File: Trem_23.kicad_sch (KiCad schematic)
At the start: 70 parts, among them J1 +9V, J2 GND, J3 IN, J4 IN GND, J5 OUT, J6 OUT GND, J7 LED SW, J8 LED GND, Q1 MMBT5089, Q2 MBT3904DW1, Q3 MBT3904DW1, Q4 MMBT3906, SW1 SQ/TRI, U1 TL064

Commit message: Trem v2.0: 9 mm pots (correct direction), RANGE switch, LFO-rate LED, 1x4 header; Unit #1 build log
As ordered from JLCPCB 2026-10-04.

Co-Authored-By: Claude Opus 5.5 <noreply@anthropic.com>
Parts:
- removed J3: IN, TestPoint:TestPoint_THTPad_D1.5mm_Drill0.7mm, symbol Connector_Generic:Conn_01x01
- removed J5: OUT, TestPoint:TestPoint_THTPad_D1.5mm_Drill0.7mm, symbol Connector_Generic:Conn_01x01
- removed J7: LED SW, TestPoint:TestPoint_THTPad_D1.5mm_Drill0.7mm, symbol Connector_Generic:Conn_01x01
- removed J8: LED GND, TestPoint:TestPoint_THTPad_D1.5mm_Drill0.7mm, symbol Connector_Generic:Conn_01x01
- added C17: 470n, Capacitor_SMD:C_0805_2012Metric_Pad1.18x1.45mm_HandSolder, symbol Device:C
- added C18: 33n, Capacitor_SMD:C_0805_2012Metric_Pad1.18x1.45mm_HandSolder, symbol Device:C
- added C19: 10n, Capacitor_SMD:C_0805_2012Metric_Pad1.18x1.45mm_HandSolder, symbol Device:C
- added C20: 100n, Capacitor_SMD:C_0805_2012Metric_Pad1.18x1.45mm_HandSolder, symbol Device:C
- added J9: IN/LED/GND/OUT, Connector_PinHeader_2.54mm:PinHeader_1x04_P2.54mm_Vertical, symbol Connector_Generic:Conn_01x04
- added Q5: MMBT3904, Package_TO_SOT_SMD:SOT-23, symbol Transistor_BJT:MMBT3904
- added R33: 2M2, Resistor_SMD:R_0805_2012Metric_Pad1.20x1.40mm_HandSolder, symbol Device:R
- added R34: 47k, Resistor_SMD:R_0805_2012Metric_Pad1.20x1.40mm_HandSolder, symbol Device:R
- added R35: 10k, Resistor_SMD:R_0805_2012Metric_Pad1.20x1.40mm_HandSolder, symbol Device:R
- added SW2: LFO/AUDIO, Trem:SW_Taiway_200_SPDT, symbol Switch:SW_SPDT
- added U2: CD4053, Package_SO:SOIC-16_3.9x9.9mm_P1.27mm, symbol Analog_Switch:CD4053B
- C14: value 10p -> 22p; LCSC C157608 -> C1804
- C3: footprint Capacitor_SMD:CP_Elec_8x10.5 -> Capacitor_THT:CP_Radial_D8.0mm_P3.50mm; now left out of the parts list
- C6: value 470n -> 10n; LCSC C13967 -> C1710
- C7: value 33n -> 1n; LCSC C1739 -> C46653
- C8: value 10n -> 220p; LCSC C1710 -> C107145
- D2, SW1: now left out of the parts list
- J1, J2, J4, J6: footprint TestPoint:TestPoint_THTPad_D1.5mm_Drill0.7mm -> Connector_Wire:SolderWire-0.5sqmm_1x01_D0.9mm_OD2.1mm
- Q2, Q3, RV4: FT Rotation Offset (none) -> 180
- Q4: value MMBT3906 -> MMBT5401; LCSC C84105 -> C8326
- R13: value 270k -> 220k; LCSC C17589 -> C17556
- R17: value 4M7 -> 2M2; LCSC C17674 -> C26113
- RV1, RV2, RV3: footprint Potentiometer_THT:Potentiometer_Omeg_PC16BU_Vertical -> Potentiometer_THT:Potentiometer_Alpha_RD901F-40-00D_Single_Vertical; now left out of the parts list
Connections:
- net +9V: now also C20.1, Q5.3 (C), R34.1, SW2.3 (C), U2.16 (VDD); no longer D2.2 (A), R13.1
- net GND: now also C20.2, J9.3 (Pin_3), SW2.1 (A), U2.6 (INH), U2.7 (VEE), U2.8 (VSS)
- net IN: now also J9.1 (Pin_1)
- net LED_K: now also J9.2 (Pin_2)
- net OUT: now also J9.4 (Pin_4)
- net SQR: now also C18.1
- net TRI: now also C17.1, R35.1
- net DEP_OUT: now reaches C8.2, R12.2, R14.1, U1.1
- net DEP_OUT: now also C19.1
- net SCH_N: now reaches C7.1, R8.2, U1.9 (-)
- net SCH_N: now also U2.1 (B1)
- net INT_N: now reaches C6.1, R5.2, U1.13 (-)
- net INT_N: now also U2.13 (A1)
- net at C10.1, Q1.1 (B), R16.2: now also R33.2; no longer R17.1
- net DEP_N: now reaches C8.1, R11.2, R12.1, R13.2, U1.2 (-)
- net DEP_N: now also U2.3 (C1)
- new net: C18.2, U2.15 (B)
- new net: SW2.2 (B), U2.10 (S2), U2.11 (S1), U2.9 (S3)
- new net: R13.1, R34.2
- new net: R17.1, R33.1
- new net: Q5.1 (B), R35.2
- new net: D2.2 (A), Q5.2 (E)
- new net: C17.2, U2.14 (A)
- new net: C19.2, U2.4 (C)
- no-connect marks 1 -> 4
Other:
- note added: "LFO: SW2 to +9V adds C17-C19 (~2-17 Hz). AUDIO: ~100-800 Hz."
- note added: "RANGE (U2 CD4053)"

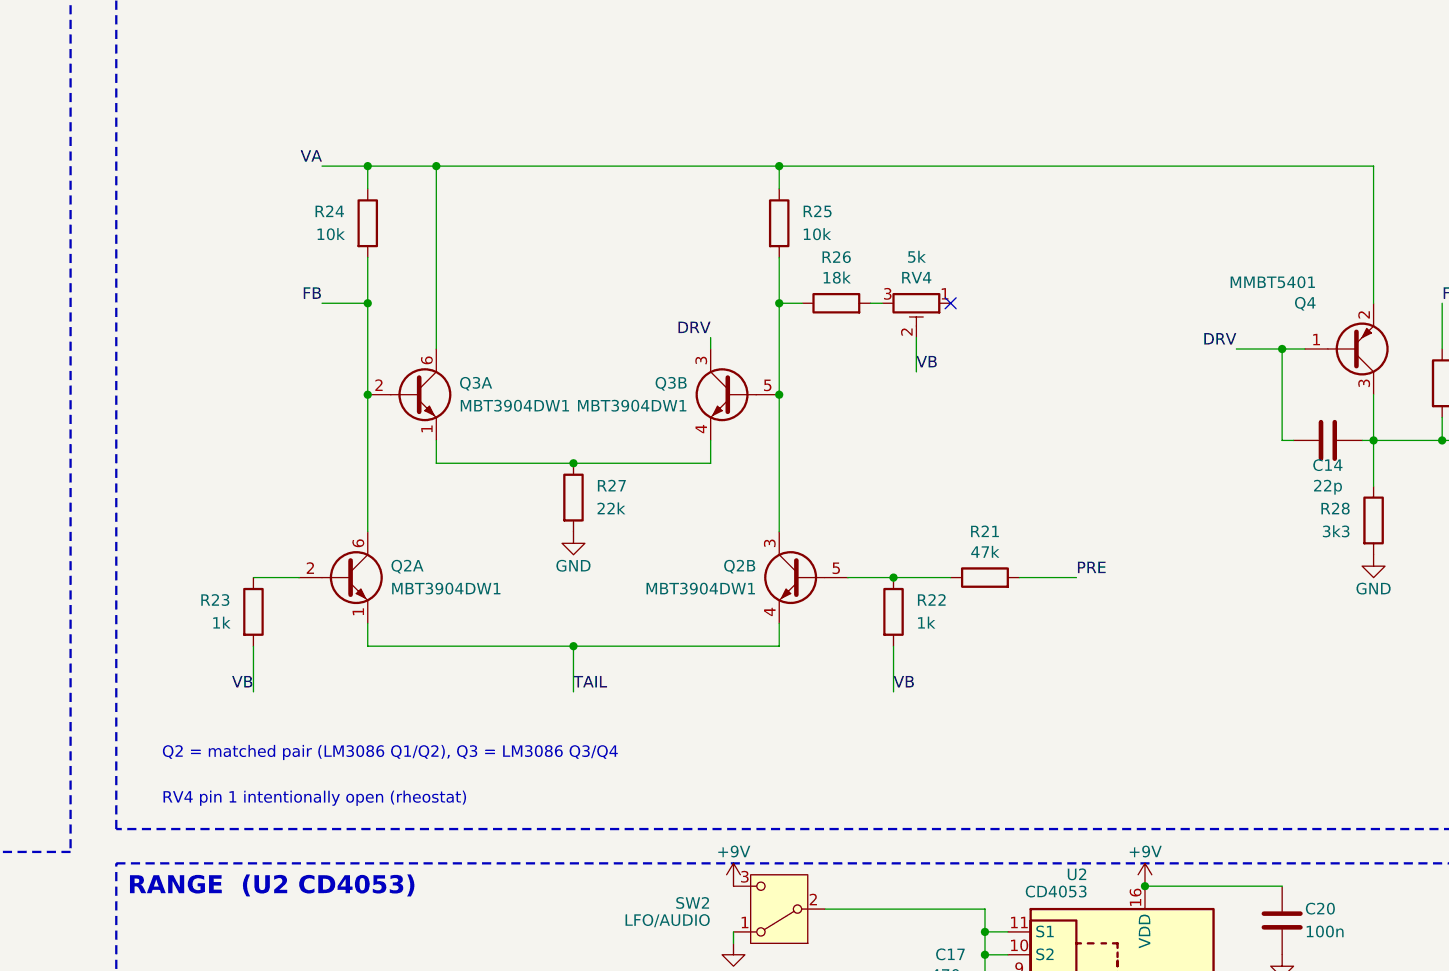
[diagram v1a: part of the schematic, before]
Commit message: v2.1 schematic: symmetric VCA balance trim (RV4 3296W 2k, wiper to VA; R26 20k to VB)
Co-Authored-By: Claude Opus 5.5 <noreply@anthropic.com>
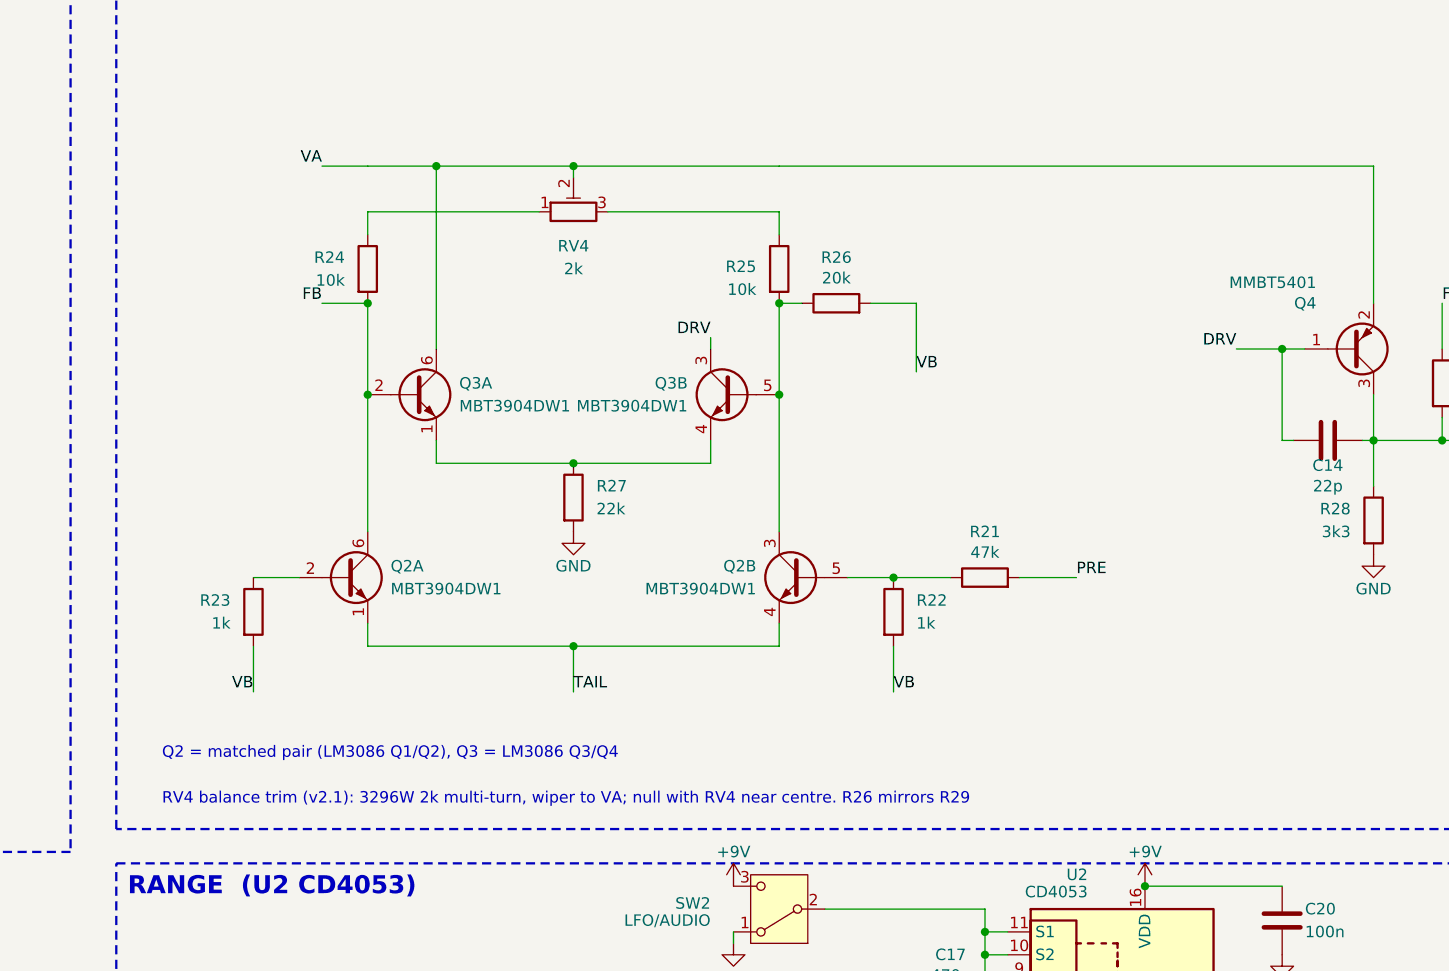
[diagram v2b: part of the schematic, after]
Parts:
- R26: value 18k -> 20k; LCSC C17506 -> C4328
- RV4: value 5k -> 2k; footprint Potentiometer_SMD:Potentiometer_Bourns_3314J_Vertical -> Potentiometer_THT:Potentiometer_Bourns_3296W_Vertical; FT Rotation Offset 180 -> (none); LCSC C58391 -> (none); now left out of the parts list
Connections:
- net VA: now also RV4.2; no longer R24.1, R25.1
- net VB: now also R26.2; no longer RV4.2
- net at RV4.3: now also R25.1; no longer R26.2
- net at RV4.1: now also R24.1
- no-connect marks 4 -> 3
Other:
- note added: "RV4 balance trim (v2.1): 3296W 2k multi-turn, wiper to VA; null with RV4 near centre. R26 mirrors R29"
- note removed: "RV4 pin 1 intentionally open (rheostat)"
- moved on the sheet: R24, R25, RV4
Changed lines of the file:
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@@
 		(title "Trem 23 - SMD")
 		(date "2026-09-24")
-		(rev "1.0")
+		(rev "2.1")
 		(comment 1 "Converted from Eagle Trem-22-01 for JLCPCB SMD assembly")
 		(comment 2 "Super-Freq.com")
@@
 		)
 	)
-	(text "RV4 pin 1 intentionally open (rheostat)"
+	(text "RV4 balance trim (v2.1): 3296W 2k multi-turn, wiper to VA; null with RV4 near centre. R26 mirrors R29"
 		(exclude_from_sim no)
 		(at 121.92 238.76 0)
@@
 	)
 	(junction
-		(at 144.78 167.64)
-		(diameter 0)
-		(color 0 0 0 0)
-	)
-	(junction
 		(at 223.52 50.8)
 		(diameter 0)
@@
 	)
 	(junction
-		(at 190.5 167.64)
-		(diameter 0)
-		(color 0 0 0 0)
-	)
-	(junction
 		(at 302.26 198.12)
 		(diameter 0)
@@
 		(color 0 0 0 0)
 	)
-	(no_connect
-		(at 209.55 182.88)
+	(junction
+		(at 167.64 167.64)
+		(diameter 0)
+		(color 0 0 0 0)
+	)
+	(wire
+		(pts
+			(xy 205.74 182.88) (xy 205.74 186.69)
+		)
+		(stroke
+			(width 0)
+			(type default)
+		)
+	)
+	(wire
+		(pts
+			(xy 200.66 182.88) (xy 205.74 182.88)
+		)
+		(stroke
+			(width 0)
+			(type default)
+		)
+	)
+	(wire
+		(pts
+			(xy 190.5 172.72) (xy 171.45 172.72)
+		)
+		(stroke
+			(width 0)
+			(type default)
+		)
+	)
+	(wire
+		(pts
+			(xy 190.5 175.26) (xy 190.5 172.72)
+		)
+		(stroke
+			(width 0)
+			(type default)
+		)
+	)
+	(wire
+		(pts
+			(xy 144.78 172.72) (xy 163.83 172.72)
+		)
+		(stroke
+			(width 0)
+			(type default)
+		)
+	)
+	(wire
+		(pts
+			(xy 144.78 175.26) (xy 144.78 172.72)
+		)
+		(stroke
+			(width 0)
+			(type default)
+		)
+	)
+	(wire
+		(pts
+			(xy 167.64 167.64) (xy 167.64 168.91)
+		)
+		(stroke
+			(width 0)
+			(type default)
+		)
+	)
+	(wire
+		(pts
+			(xy 167.64 167.64) (xy 190.5 167.64)
+		)
+		(stroke
+			(width 0)
+			(type default)
+		)
+	)
+	(wire
+		(pts
+			(xy 152.4 167.64) (xy 167.64 167.64)
+		)
+		(stroke
+			(width 0)
+			(type default)
+		)
+	)
+	(wire
+		(pts
+			(xy 190.5 208.28) (xy 190.5 182.88)
+		)
+		(stroke
+			(width 0)
+			(type default)
+		)
+	)
+	(wire
+		(pts
+			(xy 144.78 208.28) (xy 144.78 182.88)
+		)
+		(stroke
+			(width 0)
+			(type default)
+		)
 	)
 	(wire
@@
 	(wire
 		(pts
-			(xy 152.4 167.64)
-			(xy 190.5 167.64)
-		)
-		(stroke
-			(width 0)
-			(type default)
-		)
-	)
-	(wire
-		(pts
 			(xy 76.2 177.8)
 			(xy 76.2 180.34)
@@
 	(wire
 		(pts
-			(xy 190.5 170.18)
-			(xy 190.5 167.64)
-		)
-		(stroke
-			(width 0)
-			(type default)
-		)
-	)
-	(wire
-		(pts
 			(xy 381 160.02)
 			(xy 375.92 160.02)
@@
 	(wire
 		(pts
-			(xy 144.78 170.18)
-			(xy 144.78 167.64)
-		)
-		(stroke
-			(width 0)
-			(type default)
-		)
-	)
-	(wire
-		(pts
 			(xy 144.78 218.44)
 			(xy 144.78 220.98)
@@
 	(wire
 		(pts
-			(xy 144.78 208.28)
-			(xy 144.78 177.8)
-		)
-		(stroke
-			(width 0)
-			(type default)
-		)
-	)
-	(wire
-		(pts
 			(xy 252.73 55.88)
 			(xy 259.08 55.88)
@@
 	(wire
 		(pts
-			(xy 190.5 208.28)
-			(xy 190.5 177.8)
-		)
-		(stroke
-			(width 0)
-			(type default)
-		)
-	)
-	(wire
-		(pts
 			(xy 264.16 198.12)
 			(xy 270.51 198.12)
@@
 	(wire
 		(pts
-			(xy 200.66 182.88)
-			(xy 201.93 182.88)
-		)
-		(stroke
-			(width 0)
-			(type default)
-		)
-	)
-	(wire
-		(pts
 			(xy 205.74 186.69)
 			(xy 205.74 190.5)
@@
 			)
 		)
-		(property "Value" "18k"
+		(property "Value" "20k"
 			(at 196.85 180.09 90)
 			(show_name no)
@@
 			)
 		)
-		(property "Description" "Balance trim series"
+		(property "Description" "Q2B collector to VB: mirrors R29 so the trim nulls centred (v2.1)"
 			(at 196.85 182.88 90)
 			(hide yes)
@@
 			)
 		)
-		(property "LCSC" "C17506"
+		(property "LCSC" "C4328"
 			(at 196.85 182.88 90)
 			(hide yes)
@@
 	(symbol
 		(lib_id "Device:R")
-		(at 190.5 173.99 0)
+		(at 190.5 179.07 0)
 		(unit 1)
 		(body_style 1)
@@
 		(dnp no)
 		(property "Reference" "R25"
-			(at 193.04 172.72 0)
+			(at 187.96 178.82 0)
 			(show_name no)
 			(do_not_autoplace no)
@@
 					(size 1.27 1.27)
 				)
-				(justify left)
+				(justify right)
 			)
 		)
 		(property "Value" "10k"
-			(at 193.04 175.26 0)
+			(at 187.96 181.36 0)
 			(show_name no)
 			(do_not_autoplace no)
@@
 					(size 1.27 1.27)
 				)
-				(justify left)
+				(justify right)
 			)
 		)
 		(property "Footprint" "Resistor_SMD:R_0805_2012Metric"
-			(at 190.5 173.99 0)
+			(at 190.5 179.07 0)
 			(hide yes)
 			(show_name no)
@@
 		)
 		(property "Datasheet" ""
-			(at 190.5 173.99 0)
+			(at 190.5 179.07 0)
 			(hide yes)
 			(show_name no)
@@
 			)
 		)
-		(property "Description" "VCA collector load"
-			(at 190.5 173.99 0)
+		(property "Description" "VCA collector load (to RV4 end B)"
+			(at 190.5 179.07 0)
 			(hide yes)
 			(show_name no)
@@
 		)
 		(property "LCSC" "C17414"
-			(at 190.5 173.99 0)
+			(at 190.5 179.07 0)
 			(hide yes)
 			(show_name no)
@@
 	(symbol
 		(lib_id "Device:R_Potentiometer_Trim")
-		(at 205.74 182.88 270)
+		(at 167.64 172.72 90)
 		(unit 1)
 		(body_style 1)
 		(exclude_from_sim no)
-		(in_bom yes)
+		(in_bom no)
 		(on_board yes)
 		(in_pos_files yes)
 		(dnp no)
 		(property "Reference" "RV4"
-			(at 205.74 180.08 90)
+			(at 167.64 176.53 90)
 			(show_name no)
 			(do_not_autoplace no)
@@
 			)
 		)
-		(property "Value" "5k"
-			(at 205.74 177.78 90)
+		(property "Value" "2k"
+			(at 167.64 179.07 90)
 			(show_name no)
 			(do_not_autoplace no)
@@
 			)
 		)
-		(property "Footprint" "Potentiometer_SMD:Potentiometer_Bourns_3314J_Vertical"
-			(at 205.74 182.88 90)
+		(property "Footprint" "Potentiometer_THT:Potentiometer_Bourns_3296W_Vertical"
+			(at 167.64 172.72 90)
 			(hide yes)
 			(show_name no)
@@
 		)
 		(property "Datasheet" ""
-			(at 205.74 182.88 90)
+			(at 167.64 172.72 90)
 			(hide yes)
 			(show_name no)
@@
 			)
 		)
-		(property "Description" "Balance / bleed-through trim, Bourns 3314J SMD, JLC-placed (extended part)"
-			(at 205.74 182.88 90)
+		(property "Description" "VCA balance trim (v2.1): symmetric collector-load trim, wiper to VA. Bourns 3296W 2k multi-turn, THT, hand-soldered"
+			(at 167.64 172.72 90)
 			(hide yes)
 			(show_name no)
@@
 			)
 		)
-		(property "LCSC" "C58391"
-			(at 205.74 182.88 90)
+		(property "LCSC" ""
+			(at 167.64 172.72 90)
 			(hide yes)
 			(show_name no)
@@
 		(pin "3"
 		)
-		(property "FT Rotation Offset" "180"
-			(at 205.74 180.08 0)
-			(hide yes)
-			(effects
-				(font
-					(size 1.27 1.27)
-				)
-			)
-		)
 		(instances
 			(project "Trem_23"
@@
 	(symbol
 		(lib_id "Device:R")
-		(at 144.78 173.99 0)
+		(at 144.78 179.07 0)
 		(unit 1)
 		(body_style 1)
@@
 		(dnp no)
 		(property "Reference" "R24"
-			(at 142.24 172.72 0)
+			(at 142.24 177.8 0)
 			(show_name no)
 			(do_not_autoplace no)
@@
 		)
 		(property "Value" "10k"
-			(at 142.24 175.26 0)
+			(at 142.24 180.34 0)
 			(show_name no)
 			(do_not_autoplace no)
@@
 		)
 		(property "Footprint" "Resistor_SMD:R_0805_2012Metric"
-			(at 144.78 173.99 0)
+			(at 144.78 179.07 0)
 			(hide yes)
 			(show_name no)
@@
 		)
 		(property "Datasheet" ""
-			(at 144.78 173.99 0)
+			(at 144.78 179.07 0)
 			(hide yes)
 			(show_name no)
@@
 			)
 		)
-		(property "Description" "VCA collector load"
-			(at 144.78 173.99 0)
+		(property "Description" "VCA collector load (to RV4 end A)"
+			(at 144.78 179.07 0)
 			(hide yes)
 			(show_name no)
@@
 		)
 		(property "LCSC" "C17414"
-			(at 144.78 173.99 0)
+			(at 144.78 179.07 0)
 			(hide yes)
 			(show_name no)

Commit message: v2.1 PCB: RV4 back to Bourns 3314J (2k SMD, C94513, JLC-placed) for the symmetric balance trim; full re-route; fab files
The 3296W THT trimmer left 24 pads unrouted. 3314J at the v2.0 spot routes cleanly:
0 unconnected, 0 DRC errors, 67 vias.

Co-Authored-By: Claude Opus 5.5 <noreply@anthropic.com>
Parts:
- RV4: footprint Potentiometer_THT:Potentiometer_Bourns_3296W_Vertical -> Potentiometer_SMD:Potentiometer_Bourns_3314J_Vertical; FT Rotation Offset (none) -> 180; LCSC (none) -> C94513; now in the parts list
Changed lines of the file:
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@@
 		(body_style 1)
 		(exclude_from_sim no)
-		(in_bom no)
+		(in_bom yes)
 		(on_board yes)
 		(in_pos_files yes)
@@
 			)
 		)
-		(property "Footprint" "Potentiometer_THT:Potentiometer_Bourns_3296W_Vertical"
+		(property "Footprint" "Potentiometer_SMD:Potentiometer_Bourns_3314J_Vertical"
 			(at 167.64 172.72 90)
 			(hide yes)
@@
 			)
 		)
-		(property "Description" "VCA balance trim (v2.1): symmetric collector-load trim, wiper to VA. Bourns 3296W 2k multi-turn, THT, hand-soldered"
+		(property "Description" "VCA balance trim (v2.1): symmetric collector-load trim, wiper to VA. Bourns 3314J-1-202E 2k SMD, JLC-placed (extended)"
 			(at 167.64 172.72 90)
 			(hide yes)
@@
 			)
 		)
-		(property "LCSC" ""
+		(property "LCSC" "C94513"
 			(at 167.64 172.72 90)
 			(hide yes)
+			(show_name no)
+			(do_not_autoplace no)
+			(effects
+				(font
+					(size 1.27 1.27)
+				)
+			)
+		)
+		(property "FT Rotation Offset" "180"
+			(at 167.64 172.72 90)
+			(hide yes)
